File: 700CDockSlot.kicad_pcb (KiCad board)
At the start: 2 copper layers, 94 x 77 mm, 21 parts, among them J1 BUS_MCA, J10 GND, J100 Conn_02x60, J2 UPPER, J3 HPLA_PORT, J4 HPLA_PORT, J5 HPLA_PORT, J6 HPLA_PORT, J7 IRQ, J8 5V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

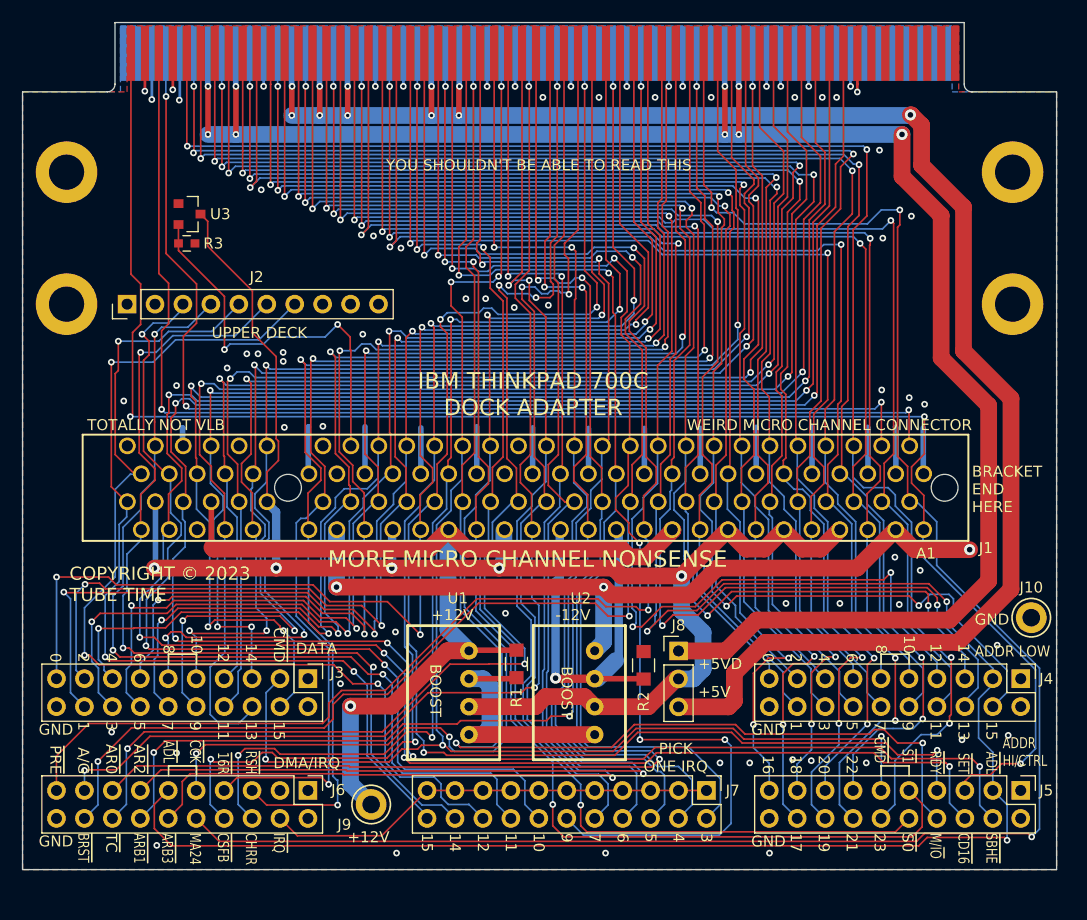
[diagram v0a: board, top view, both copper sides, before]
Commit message: Rev 2: Fix CHRESET, disconnect and pull up MADE24
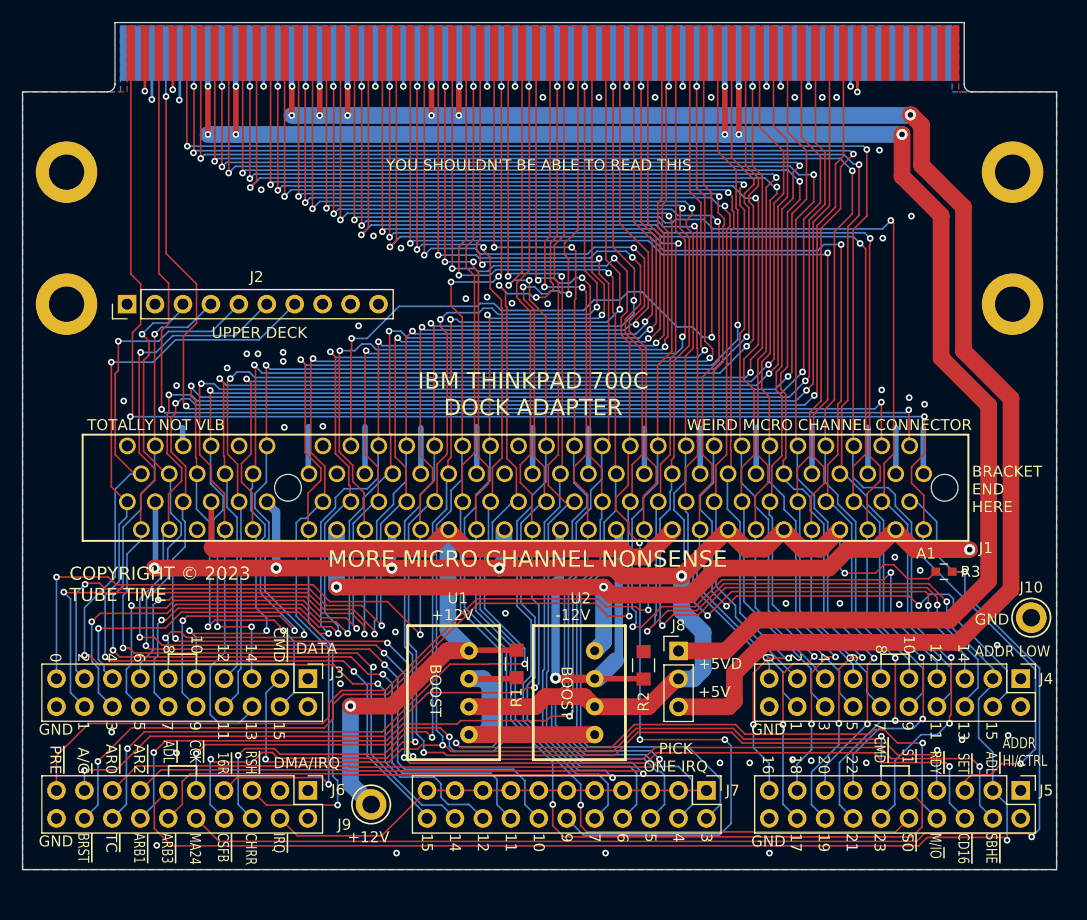
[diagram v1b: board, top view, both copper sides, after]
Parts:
- removed U3: MAX810LTRG, Active:SOT95P230X117-3
- moved R3 75.0 mm to (175.3, 95.1)
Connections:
- J100 pad 102: /MADE24 -> /CHRST
- R3 pad 1: /CHRST -> +5C
- R3 pad 2: GND -> /MADE24
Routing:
- net /MADE24: track 173.0 -> 115.2 mm, vias 3 -> 2
- net /CHRST: track 35.9 -> 72.8 mm
- net +5C: track 148.9 -> 132.9 mm, vias 5 -> 6
